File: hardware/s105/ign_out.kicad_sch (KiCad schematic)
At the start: 10 parts

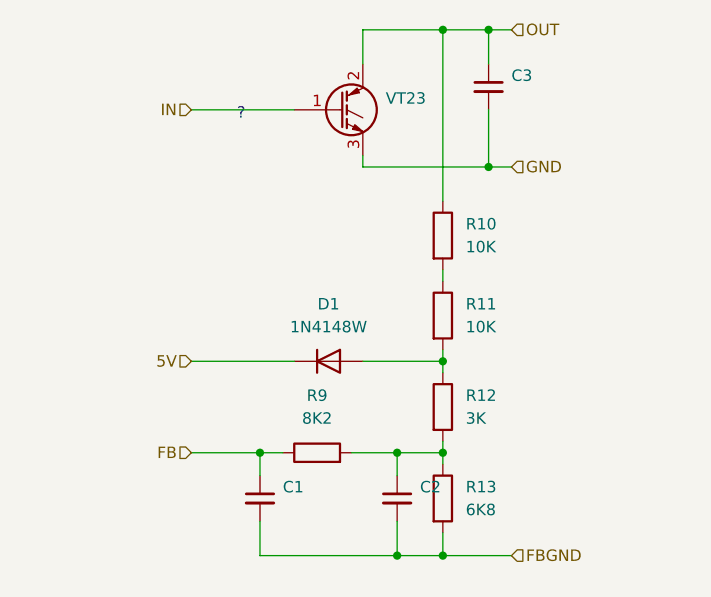
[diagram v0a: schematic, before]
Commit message: разместила схожие блоки
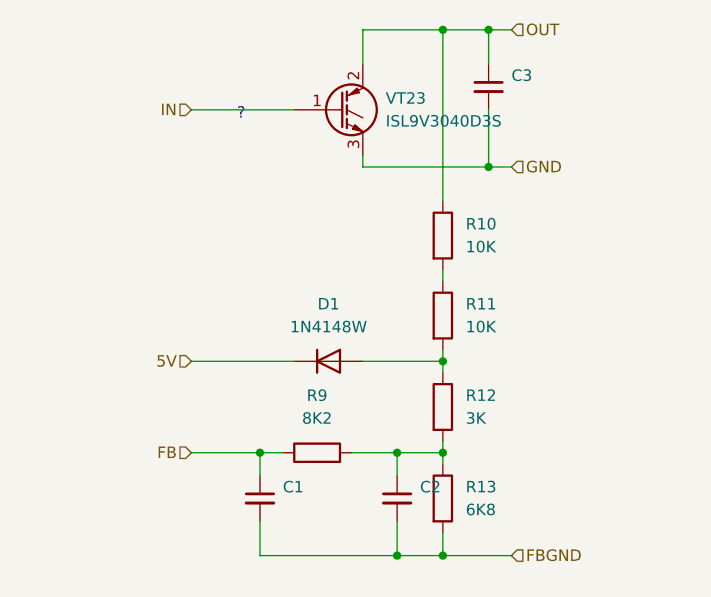
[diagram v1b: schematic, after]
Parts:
- VT23: value (none) -> ISL9V3040D3S; footprint (none) -> Package_TO_SOT_SMD:TO-252-2
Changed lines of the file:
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@@
       (effects (font (size 1.27 1.27)) (justify left))
     )
-    (property "Value" "" (id 1) (at 175.26 77.4699 0)
+    (property "Value" "ISL9V3040D3S" (id 1) (at 175.26 77.4699 0)
       (effects (font (size 1.27 1.27)) (justify left))
     )
-    (property "Footprint" "" (id 2) (at 175.26 78.105 0)
+    (property "Footprint" "Package_TO_SOT_SMD:TO-252-2" (id 2) (at 175.26 78.105 0)
       (effects (font (size 1.27 1.27) italic) (justify left) hide)
     )

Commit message: вписала в габариты платы, продолжила опознание
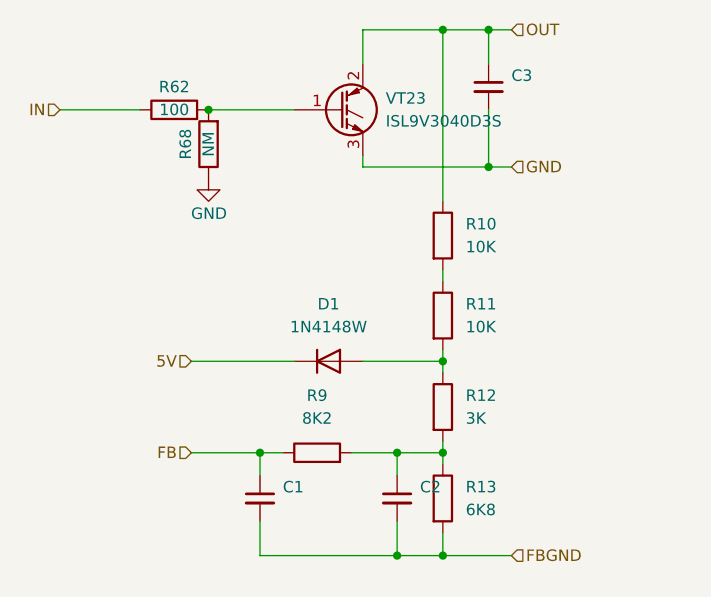
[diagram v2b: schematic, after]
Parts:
- added R62: 100, Resistor_SMD:R_0603_1608Metric, symbol Device:R
- added R68: NM, Resistor_SMD:R_0603_1608Metric, symbol Device:R
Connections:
- net GND: now also R68.1
- net IN: now also R62.1; no longer VT23.1 (G)
- new net: R62.2, R68.2, VT23.1 (G)
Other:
- note removed: "?"
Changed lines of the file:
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@@
 (kicad_sch (version 20211123) (generator eeschema)
   (paper "A4")
+  (junction (at 155.575 76.2) (diameter 0) (color 0 0 0 0)
+  )
   (junction (at 176.53 125.73) (diameter 0) (color 0 0 0 0)
   )
@@
     (stroke (width 0) (type default) (color 0 0 0 0))
   )
-  (wire (pts (xy 153.67 76.2) (xy 165.1 76.2))
+  (wire (pts (xy 139.065 76.2) (xy 147.955 76.2))
     (stroke (width 0) (type default) (color 0 0 0 0))
   )
@@
     (stroke (width 0) (type default) (color 0 0 0 0))
   )
+  (wire (pts (xy 155.575 76.2) (xy 165.1 76.2))
+    (stroke (width 0) (type default) (color 0 0 0 0))
+  )
   (wire (pts (xy 181.61 104.14) (xy 181.61 105.41))
     (stroke (width 0) (type default) (color 0 0 0 0))
-  )
-  (text "?" (at 158.75 77.47 0)
-    (effects (font (size 1.27 1.27)) (justify left bottom))
   )
   (hierarchical_label "GND" (shape input) (at 189.23 82.55 0)
@@
     (effects (font (size 1.27 1.27)) (justify left))
   )
-  (hierarchical_label "IN" (shape input) (at 153.67 76.2 180)
+  (hierarchical_label "IN" (shape input) (at 139.065 76.2 180)
     (effects (font (size 1.27 1.27)) (justify right))
   )
@@
     (pin "2")
   )
+  (symbol (lib_id "Device:R") (at 151.765 76.2 90) (unit 1)
+    (in_bom yes) (on_board yes)
+    (property "Reference" "R62" (id 0) (at 151.765 73.66 90))
+    (property "Value" "100" (id 1) (at 151.765 76.2 90))
+    (property "Footprint" "Resistor_SMD:R_0603_1608Metric" (id 2) (at 151.765 77.978 90)
+      (effects (font (size 1.27 1.27)) hide)
+    )
+    (property "Datasheet" "~" (id 3) (at 151.765 76.2 0)
+      (effects (font (size 1.27 1.27)) hide)
+    )
+    (pin "1")
+    (pin "2")
+  )
   (symbol (lib_id "Device:C_Small") (at 161.29 119.38 0) (unit 1)
     (in_bom yes) (on_board yes) (fields_autoplaced)
@@
     (pin "1")
     (pin "2")
+  )
+  (symbol (lib_id "power:GND") (at 155.575 83.82 0) (unit 1)
+    (in_bom yes) (on_board yes)
+    (property "Reference" "#PWR0189" (id 0) (at 155.575 90.17 0)
+      (effects (font (size 1.27 1.27)) hide)
+    )
+    (property "Value" "GND" (id 1) (at 153.6307 87.7294 0)
+      (effects (font (size 1.27 1.27)) (justify left))
+    )
+    (property "Footprint" "" (id 2) (at 155.575 83.82 0)
+      (effects (font (size 1.27 1.27)) hide)
+    )
+    (property "Datasheet" "" (id 3) (at 155.575 83.82 0)
+      (effects (font (size 1.27 1.27)) hide)
+    )
+    (pin "1")
   )
   (symbol (lib_name "R_1") (lib_id "Device:R") (at 167.64 114.3 90) (unit 1)
@@
       (effects (font (size 1.27 1.27)) hide)
     )
+    (pin "1")
+    (pin "2")
+  )
+  (symbol (lib_id "Device:R") (at 155.575 80.01 180) (unit 1)
+    (in_bom yes) (on_board yes)
+    (property "Reference" "R68" (id 0) (at 153.035 80.01 90))
+    (property "Value" "NM" (id 1) (at 155.575 80.01 90))
+    (property "Footprint" "Resistor_SMD:R_0603_1608Metric" (id 2) (at 157.353 80.01 90)
+      (effects (font (size 1.27 1.27)) hide)
+    )
+    (property "Datasheet" "~" (id 3) (at 155.575 80.01 0)
+      (effects (font (size 1.27 1.27)) hide)
+    )

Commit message: +knock
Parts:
- R62: value 100 -> 10
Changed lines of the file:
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@@
     (in_bom yes) (on_board yes)
     (property "Reference" "R62" (id 0) (at 151.765 73.66 90))
-    (property "Value" "100" (id 1) (at 151.765 76.2 90))
+    (property "Value" "10" (id 1) (at 151.765 76.2 90))
     (property "Footprint" "Resistor_SMD:R_0603_1608Metric" (id 2) (at 151.765 77.978 90)
       (effects (font (size 1.27 1.27)) hide)

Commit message: закончила пока что
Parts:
- added D66: BAV99, Package_TO_SOT_SMD:SOT-23, symbol Diode:BAV99
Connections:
- net GND: now also D66.1 (K)
- net at C2.1, R12.2, R13.1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: now also D66.3 (K)
- new net +3.3V: D66.2 (A)
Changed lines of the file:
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@@
+    (stroke (width 0) (type default) (color 0 0 0 0))
+  )
+  (wire (pts (xy 181.61 114.3) (xy 194.945 114.3))
     (stroke (width 0) (type default) (color 0 0 0 0))
   )
@@
     (pin "2")
   )
+  (symbol (lib_id "Diode:BAV99") (at 200.025 114.3 270) (mirror x) (unit 1)
+    (in_bom yes) (on_board yes) (fields_autoplaced)
+    (property "Reference" "D66" (id 0) (at 202.565 113.0299 90)
+      (effects (font (size 1.27 1.27)) (justify left))
+    )
+    (property "Value" "BAV99" (id 1) (at 202.565 115.5699 90)
+      (effects (font (size 1.27 1.27)) (justify left))
+    )
+    (property "Footprint" "Package_TO_SOT_SMD:SOT-23" (id 2) (at 187.325 114.3 0)
+      (effects (font (size 1.27 1.27)) hide)
+    )
+    (property "Datasheet" "https://assets.nexperia.com/documents/data-sheet/BAV99_SER.pdf" (id 3) (at 200.025 114.3 0)
+      (effects (font (size 1.27 1.27)) hide)
+    )
+    (pin "1")
+    (pin "2")
+    (pin "3")
+  )
   (symbol (lib_id "Transistor_IGBT:IRG4PF50W") (at 170.18 76.2 0) (unit 1)
     (in_bom yes) (on_board yes) (fields_autoplaced)
@@
     (pin "2")
   )
+  (symbol (lib_id "power:GND") (at 200.025 121.92 0) (unit 1)
+    (in_bom yes) (on_board yes) (fields_autoplaced)
+    (property "Reference" "#PWR0181" (id 0) (at 200.025 128.27 0)
+      (effects (font (size 1.27 1.27)) hide)
+    )
+    (property "Value" "GND" (id 1) (at 200.025 127 0))
+    (property "Footprint" "" (id 2) (at 200.025 121.92 0)
+      (effects (font (size 1.27 1.27)) hide)
+    )
+    (property "Datasheet" "" (id 3) (at 200.025 121.92 0)
+      (effects (font (size 1.27 1.27)) hide)
+    )
+    (pin "1")
+  )
   (symbol (lib_name "R_1") (lib_id "Device:R") (at 181.61 119.38 0) (unit 1)
     (in_bom yes) (on_board yes) (fields_autoplaced)
@@
     (pin "2")
   )
+  (symbol (lib_id "power:+3.3V") (at 200.025 106.68 0) (unit 1)
+    (in_bom yes) (on_board yes) (fields_autoplaced)
+    (property "Reference" "#PWR0423" (id 0) (at 200.025 110.49 0)
+      (effects (font (size 1.27 1.27)) hide)
+    )
+    (property "Value" "+3.3V" (id 1) (at 200.025 101.6 0))
+    (property "Footprint" "" (id 2) (at 200.025 106.68 0)
+      (effects (font (size 1.27 1.27)) hide)
+    )
+    (property "Datasheet" "" (id 3) (at 200.025 106.68 0)
+      (effects (font (size 1.27 1.27)) hide)
+    )
+    (pin "1")
+  )
 )

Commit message: #4 #5 #6 #8
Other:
- company: (none) -> rusEFI
- title: (none) -> s105
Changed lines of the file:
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@@
 (kicad_sch (version 20211123) (generator eeschema)
-  (paper "A4")
+  (paper "A3" portrait)
+  (title_block
+    (title "s105")
+    (rev "0.1")
+    (company "rusEFI")
+  )
   (junction (at 155.575 76.2) (diameter 0) (color 0 0 0 0)
   )
